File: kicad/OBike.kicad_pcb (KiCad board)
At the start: 4 copper layers, 60 x 99.2 mm, 65 parts, among them J1 62684-402100ALF, J2 Micro_SD_Card_Det1, J3 Conn_01x02, J5 U.FL-R-SMT-1_10_, SW1 5_position_tactile, U1 DPS368XTSA1, U10 MAX40200AUK, U2 DS3231M, U3 MCP23017_SO, U4 74HC14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

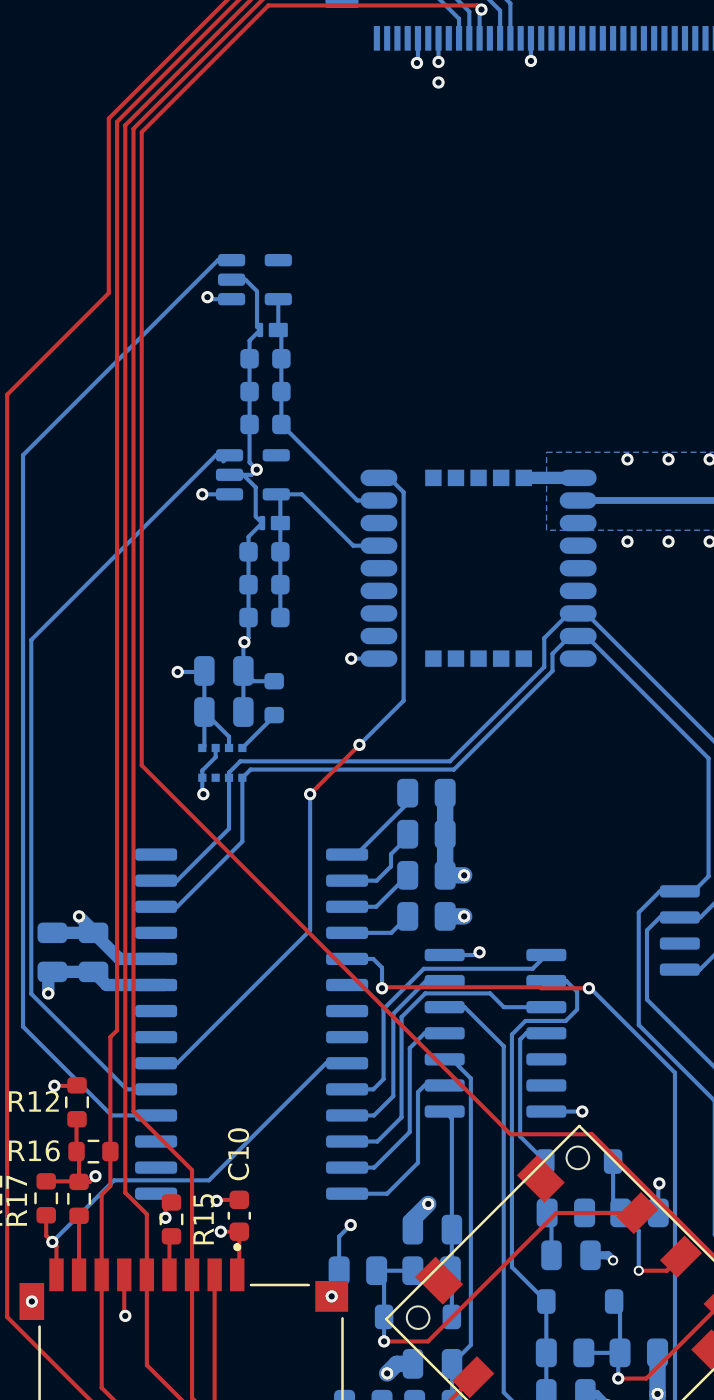
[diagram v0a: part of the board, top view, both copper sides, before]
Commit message: migrate to platform IO
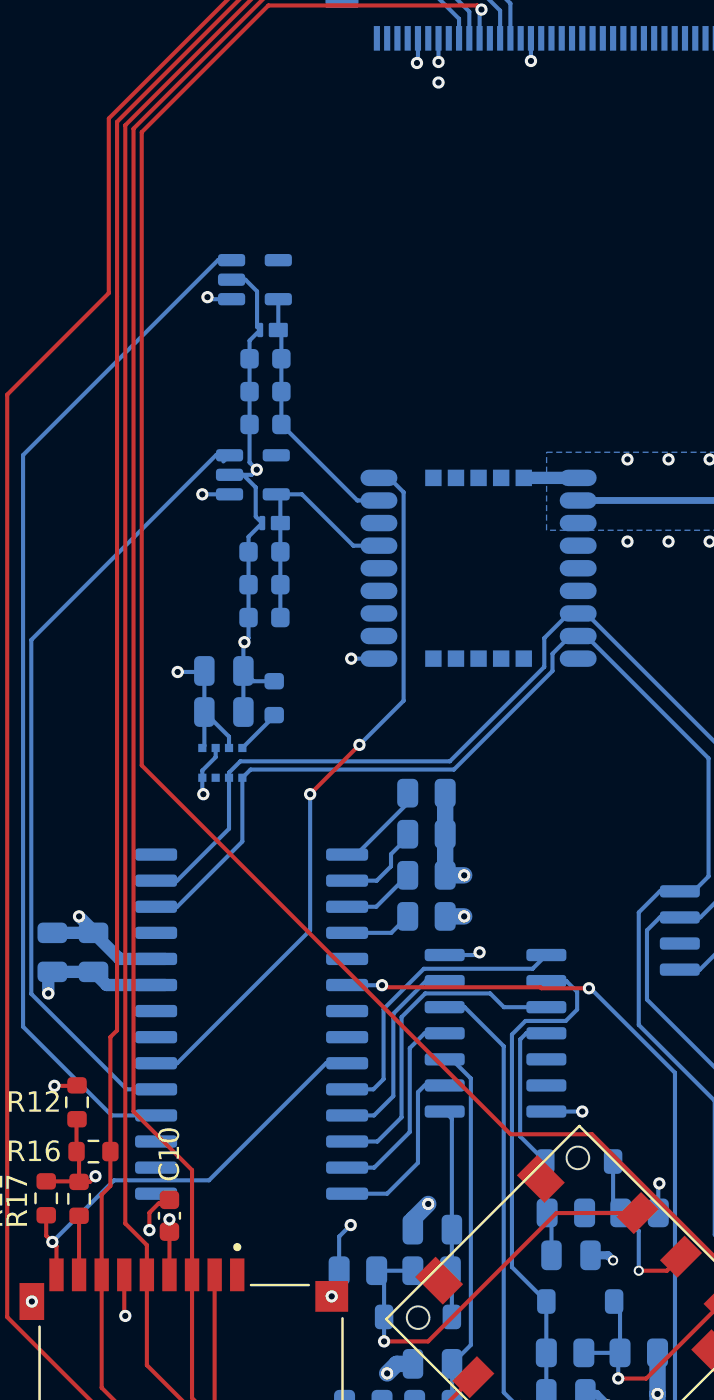
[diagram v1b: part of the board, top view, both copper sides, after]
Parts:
- removed R15: 100K, Resistor_SMD:R_0603_1608Metric
- moved C10 3.40 mm to (128.2, 118.3)
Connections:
- C10 pad 1: Net-(J2-DAT2) -> Net-(J2-VDD)
- J2 pad 1: Net-(J2-DAT2) -> unconnected-(J2-DAT2-Pad1)
- J2 pad CD: CD -> (no net)
- J2 pad G1: GND -> (no net)
- J2 pad G2: GND -> (no net)
- J2 pad G3: GND -> (no net)
- J2 pad G4: GND -> (no net)
- R11 pad 1: Net-(J2-DAT2) -> Net-(J2-VDD)
- R12 pad 2: Net-(J2-DAT2) -> Net-(J2-VDD)
- R16 pad 1: Net-(J2-DAT2) -> Net-(J2-VDD)
- R17 pad 1: Net-(J2-DAT2) -> Net-(J2-VDD)
- U3 pad 19: INT -> unconnected-(U3-INTB-Pad19)
- U3 pad 20: unconnected-(U3-INTA-Pad20) -> INT
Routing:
- net Net-(J2-DAT2): track 16.9 -> 0.00 mm, vias 3 -> 0
- net Net-(J2-VDD): track 2.03 -> 15.7 mm, vias 0 -> 2
- net INT: track 40.1 -> 39.0 mm
- net GND: track 99.5 -> 100.4 mm

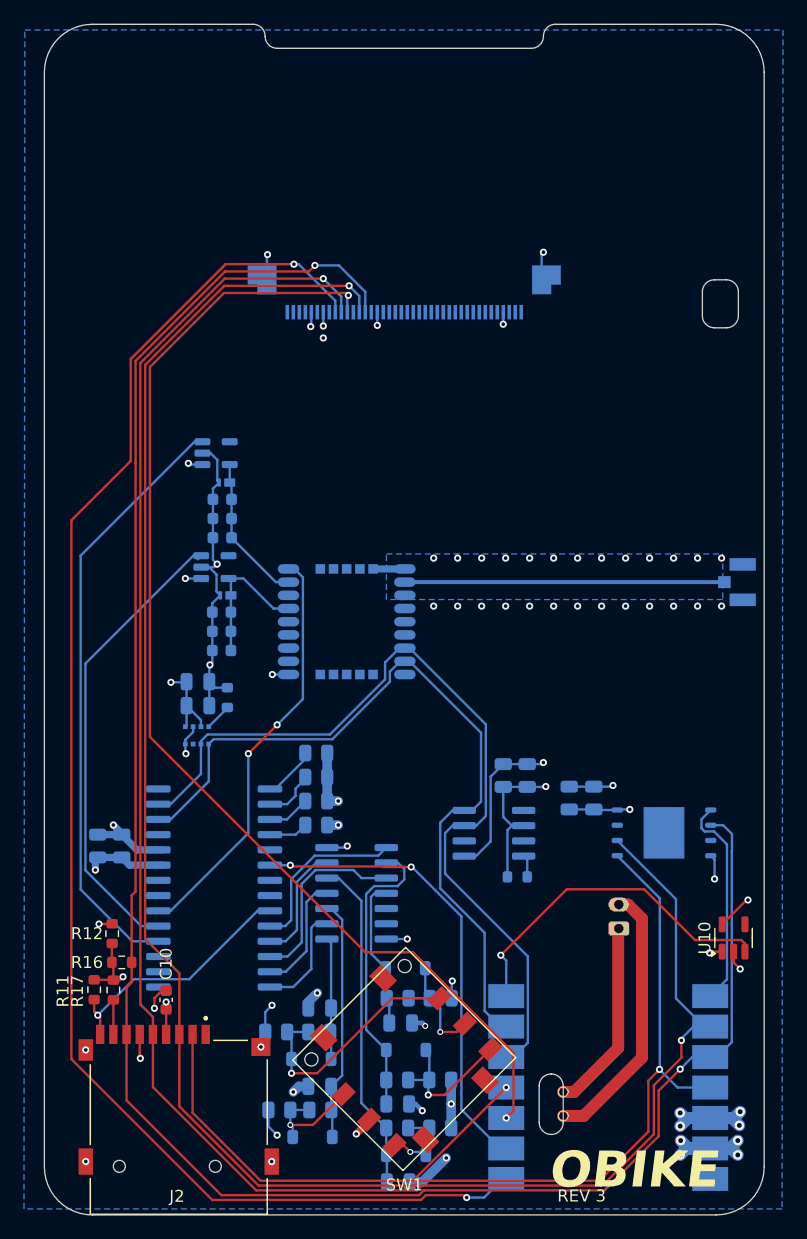
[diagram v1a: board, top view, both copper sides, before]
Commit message: LCD interface
fixed mistakes in FPC connector nets
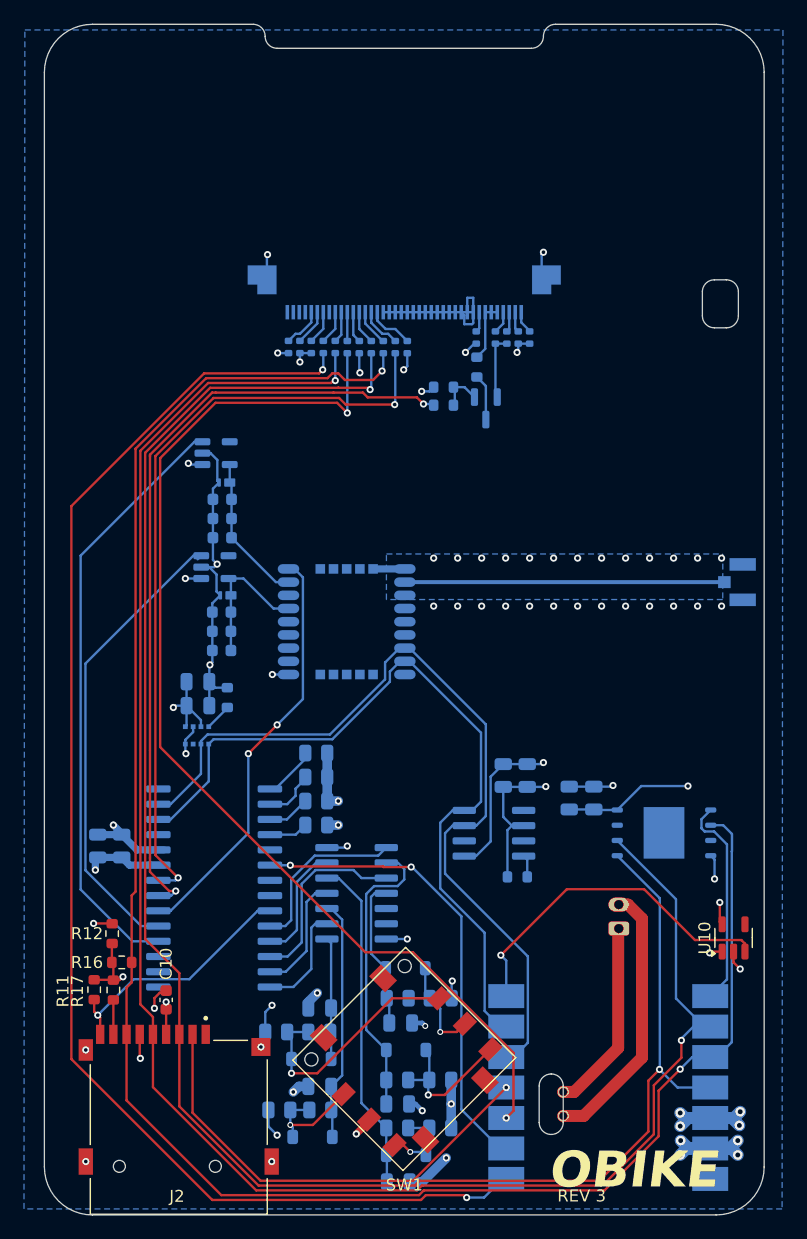
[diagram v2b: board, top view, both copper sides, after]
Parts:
- added Q1: SS8050, Package_TO_SOT_SMD:SOT-23, B.Cu at (154.8, 69.0)
- added R15: 0R, Resistor_SMD:R_0402_1005Metric, B.Cu at (139.3, 63.9)
- added R18: 0R, Resistor_SMD:R_0402_1005Metric, B.Cu at (157.6, 63.1)
- added R19: 0R, Resistor_SMD:R_0402_1005Metric, B.Cu at (158.5, 63.1)
- added R20: 0R, Resistor_SMD:R_0402_1005Metric, B.Cu at (156.6, 63.1)
- added R21: 0R, Resistor_SMD:R_0402_1005Metric, B.Cu at (140.3, 63.9)
- added R26: 0R, Resistor_SMD:R_0402_1005Metric, B.Cu at (141.3, 63.9)
- added R27: 0R, Resistor_SMD:R_0402_1005Metric, B.Cu at (142.3, 63.9)
- added R28: 0R, Resistor_SMD:R_0402_1005Metric, B.Cu at (143.3, 63.9)
- added R29: 0R, Resistor_SMD:R_0402_1005Metric, B.Cu at (144.3, 63.9)
- added R30: 0R, Resistor_SMD:R_0402_1005Metric, B.Cu at (145.3, 63.9)
- added R31: 0R, Resistor_SMD:R_0402_1005Metric, B.Cu at (146.3, 63.9)
- added R32: 0R, Resistor_SMD:R_0402_1005Metric, B.Cu at (147.3, 63.9)
- added R33: 0R, Resistor_SMD:R_0402_1005Metric, B.Cu at (148.3, 63.9)
- added R34: 0R, Resistor_SMD:R_0402_1005Metric, B.Cu at (138.4, 63.9)
- added R35: 0R, Resistor_SMD:R_0402_1005Metric, B.Cu at (155.7, 63.1)
- added R36: 47R, Resistor_SMD:R_0603_1608Metric, B.Cu at (154.1, 65.6)
- added R37: 10K, Resistor_SMD:R_0603_1608Metric, B.Cu at (151.3, 67.2)
- added R38: 1K, Resistor_SMD:R_0603_1608Metric, B.Cu at (151.3, 68.8)
- added R39: 0R, Resistor_SMD:R_0402_1005Metric, B.Cu at (154.1, 63.1)
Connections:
- J1 pad 05: GND -> Net-(J1-Pad05)
- J1 pad 06: unconnected-(J1-Pad06) -> Net-(J1-Pad06)
- J1 pad 07: AUX_3V3 -> Net-(J1-Pad07)
- J1 pad 09: SCR_CS -> Net-(J1-Pad09)
- J1 pad 10: SCK -> Net-(J1-Pad10)
- J1 pad 11: SCR_DC -> Net-(J1-Pad11)
- J1 pad 12: unconnected-(J1-Pad12) -> Net-(J1-Pad12)
- J1 pad 13: MOSI -> Net-(J1-Pad13)
- J1 pad 14: MISO -> Net-(J1-Pad14)
- J1 pad 15: unconnected-(J1-Pad15) -> Net-(J1-Pad15)
- J1 pad 16: GND -> Net-(J1-Pad16)
- J1 pad 17: unconnected-(J1-Pad17) -> GND
- J1 pad 18: unconnected-(J1-Pad18) -> GND
- J1 pad 19: unconnected-(J1-Pad19) -> GND
- J1 pad 20: unconnected-(J1-Pad20) -> GND
- J1 pad 21: unconnected-(J1-Pad21) -> GND
- J1 pad 22: unconnected-(J1-Pad22) -> GND
- J1 pad 23: unconnected-(J1-Pad23) -> GND
- J1 pad 24: unconnected-(J1-Pad24) -> GND
- J1 pad 25: unconnected-(J1-Pad25) -> GND
- J1 pad 26: unconnected-(J1-Pad26) -> GND
- J1 pad 27: unconnected-(J1-Pad27) -> GND
- J1 pad 28: unconnected-(J1-Pad28) -> GND
- J1 pad 29: unconnected-(J1-Pad29) -> GND
- J1 pad 30: unconnected-(J1-Pad30) -> GND
- J1 pad 31: unconnected-(J1-Pad31) -> GND
- J1 pad 32: unconnected-(J1-Pad32) -> GND
- J1 pad 33: unconnected-(J1-Pad33) -> Net-(J1-Pad33)
- J1 pad 34: unconnected-(J1-Pad34) -> Net-(J1-Pad34)
- J1 pad 35: unconnected-(J1-Pad35) -> Net-(J1-Pad34)
- J1 pad 36: unconnected-(J1-Pad36) -> Net-(J1-Pad34)
- J1 pad 37: GND -> Net-(J1-Pad37)
- J1 pad 38: unconnected-(J1-Pad38) -> Net-(J1-Pad38)
- J1 pad 39: unconnected-(J1-Pad39) -> Net-(J1-Pad39)
- J1 pad 40: unconnected-(J1-Pad40) -> Net-(J1-Pad40)
- J2 pad CD: (no net) -> CD
- J2 pad G1: (no net) -> GND
- J2 pad G2: (no net) -> GND
- J2 pad G3: (no net) -> GND
- J2 pad G4: (no net) -> GND
- U3 pad 7: SCR_BL -> SCR_BK
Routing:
- net SCR_BK: track 0.00 -> 65.5 mm, vias 0 -> 2
- net SCR_RST: track 0.00 -> 64.2 mm, vias 0 -> 2
- net AUX_3V3: track 225.5 -> 246.9 mm, vias 5 -> 7
- net GND: track 100.4 -> 121.0 mm, vias 58 -> 59
- net SCR_CS: track 124.9 -> 115.2 mm
- net SCK: track 160.4 -> 152.5 mm
- net MISO: track 167.7 -> 160.5 mm
- net SCR_DC: track 98.3 -> 92.6 mm
- net MOSI: track 158.6 -> 153.2 mm
- net Net-(J1-Pad34): track 0.00 -> 5.04 mm
- net Net-(J1-Pad16): track 0.00 -> 3.90 mm
- net Net-(Q1-C): track 0.00 -> 3.86 mm
- net Net-(Q1-B): track 0.00 -> 3.54 mm
- net Net-(J1-Pad15): track 0.00 -> 3.51 mm
- net Net-(J1-Pad05): track 0.00 -> 3.39 mm
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
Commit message: screen fpc
- changed fpc to bottom mount pins
- changed fpc footprint and symbol
- updated fpc routing
- added JST connectors for SPI & I2C expansion
- stopped tracking kicad/*.zip
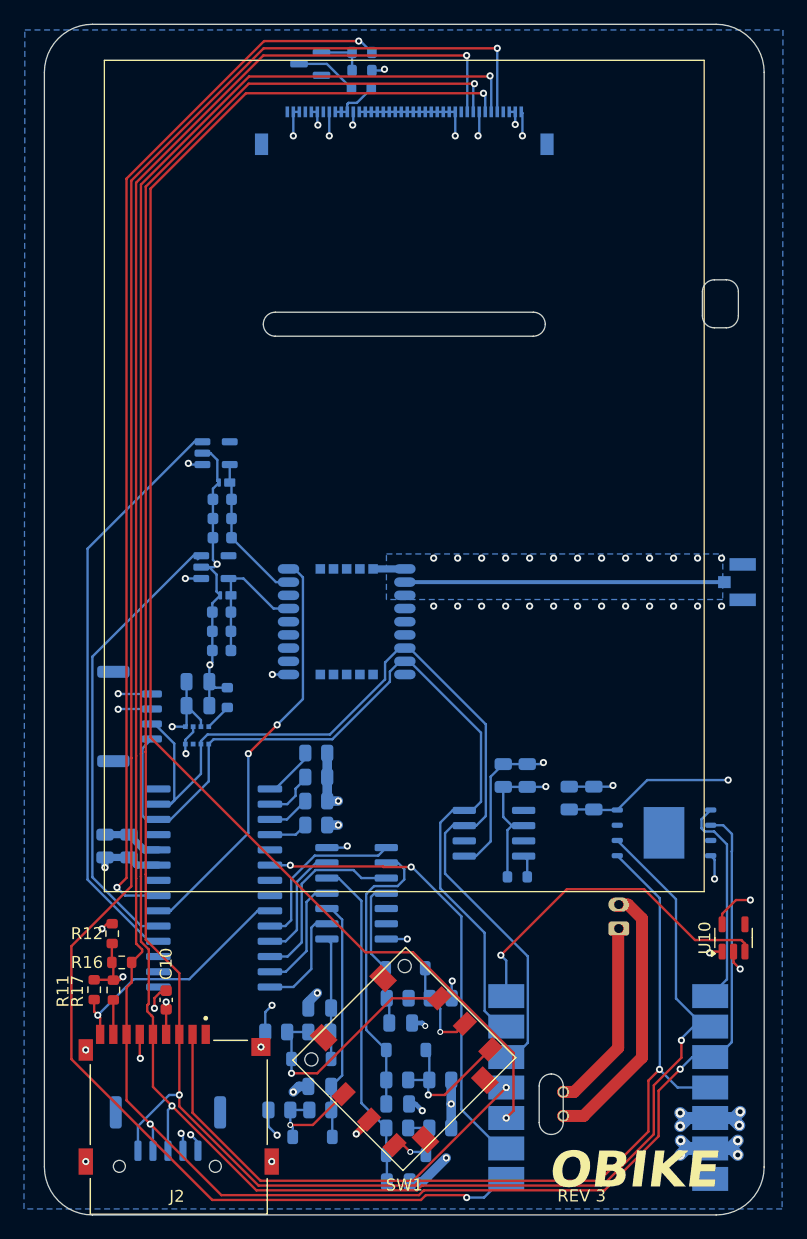
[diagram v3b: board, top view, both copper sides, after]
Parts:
- removed R15, R18, R19, R20, R21, R26, R27, R28, R29, R30, R31, R32, R33, R34, R35, R39: 0R, Resistor_SMD:R_0402_1005Metric
- added J4: Conn_01x04, Connector_JST:JST_GH_SM04B-GHS-TB_1x04-1MP_P1.25mm_Horizontal, B.Cu at (125.2, 94.7)
- added J7: Conn_01x05, Connector_JST:JST_GH_SM05B-GHS-TB_1x05-1MP_P1.25mm_Horizontal, B.Cu at (128.3, 129.1)
- J1: value 62684-402100ALF -> F34G-1A7Q1-E8C40; footprint amphenol:AMPHENOL_62684-402100ALF -> amphenol:AMPHENOL_F34G-1A7Q1-E8C40
- moved Q1 32.2 mm to (140.2, 40.3), turned to 180 degrees
- moved R38 30.2 mm to (144.5, 39.4), turned to 180 degrees
- moved R37 27.3 mm to (144.5, 40.9), turned to 180 degrees
- moved R36 25.1 mm to (144.5, 42.4), turned to 0 degrees
- moved J1 10.4 mm to (148.1, 47.0), turned to 180 degrees
- moved C11 0.60 mm to (125.1, 105.5)
- moved C12 0.60 mm to (123.1, 105.5)
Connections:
- J1 pad 10: Net-(J1-Pad10) -> MISO
- J1 pad 11: Net-(J1-Pad11) -> SCR_RST
- J1 pad 12: Net-(J1-Pad12) -> GND
- J1 pad 13: Net-(J1-Pad13) -> GND
- J1 pad 14: Net-(J1-Pad14) -> GND
- J1 pad 15: Net-(J1-Pad15) -> GND
- J1 pad 16: Net-(J1-Pad16) -> GND
- J1 pad 29: GND -> AUX_3V3
- J1 pad 30: GND -> Net-(J1-Pad30)
- J1 pad 31: GND -> Net-(J1-Pad30)
- J1 pad 32: GND -> Net-(J1-Pad30)
- J1 pad 33: Net-(J1-Pad33) -> GND
- J1 pad 34: Net-(J1-Pad34) -> GND
- J1 pad 35: Net-(J1-Pad34) -> AUX_3V3
- J1 pad 36: Net-(J1-Pad34) -> AUX_3V3
- J1 pad 37: Net-(J1-Pad37) -> unconnected-(J1-Pad37)
- J1 pad 38: Net-(J1-Pad38) -> GND
- J1 pad 39: Net-(J1-Pad39) -> GND
- J1 pad 40: Net-(J1-Pad40) -> unconnected-(J1-Pad40)
- J2 pad CD: CD -> (no net)
- J2 pad G1: GND -> (no net)
- J2 pad G2: GND -> (no net)
- J2 pad G3: GND -> (no net)
- J2 pad G4: GND -> (no net)
- R36 pad 2: Net-(J1-Pad34) -> Net-(J1-Pad30)
- U3 pad 8: SCR_RST -> unconnected-(U3-GPB7-Pad8)
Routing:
- net SCR_RST: track 64.2 -> 0.00 mm, vias 2 -> 0
- net SCR_CS: track 115.2 -> 157.7 mm
- net SCK: track 152.5 -> 193.5 mm, vias 2 -> 3
- net MOSI: track 153.2 -> 191.1 mm, vias 2 -> 3
- net MISO: track 160.5 -> 196.9 mm, vias 2 -> 3
- net SCR_DC: track 92.6 -> 125.2 mm
- net SCR_BK: track 65.5 -> 88.7 mm
- net AUX_3V3: track 246.9 -> 261.5 mm
- net SCL: track 66.6 -> 74.7 mm
- net SDA: track 72.0 -> 79.7 mm
- net GND: track 121.0 -> 115.0 mm, vias 59 -> 60
- net Net-(J1-Pad34): track 5.04 -> 0.00 mm
- net Net-(J1-Pad30): track 0.00 -> 4.19 mm
- net Net-(J1-Pad16): track 3.90 -> 0.00 mm
- net Net-(J1-Pad15): track 3.51 -> 0.00 mm
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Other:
- outline, holes or cut-outs redrawn

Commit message: pcb update
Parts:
- removed the ? at (161.3, 126.0)
- removed the ? at (161.3, 128.0)
- added ?: , , F.Cu at (163.9, 128.0)
- added LS1: PK-11N40PQ, Mallory:PK-11N40PQ_MAL, B.Cu at (123.1, 46.0)
- added REF**: TestPoint_Pad_1.0x1.0mm, TestPoint:TestPoint_Pad_1.0x1.0mm, F.Cu at (163.9, 126.0)
- J4: footprint Connector_JST:JST_GH_SM04B-GHS-TB_1x04-1MP_P1.25mm_Horizontal -> Connector_PinHeader_2.54mm:PinHeader_1x04_P2.54mm_Vertical; moved to F.Cu
- J7: footprint Connector_JST:JST_GH_SM05B-GHS-TB_1x05-1MP_P1.25mm_Horizontal -> Connector_PinHeader_2.54mm:PinHeader_1x05_P2.54mm_Vertical; moved to F.Cu
- moved J7 95.4 mm to (174.0, 45.2), turned to -90 degrees
- moved R12 5.53 mm to (120.7, 117.5), turned to 90 degrees
- moved R16 2.44 mm to (125.3, 117.5), turned to 90 degrees
- moved J4 1.33 mm to (123.8, 94.4), turned to 0 degrees
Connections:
- J1 pad 1: GND -> unconnected-(J1-Pad1)
- J1 pad 10: MISO -> SCK
- J1 pad 11: SCR_RST -> SCR_DC
- J1 pad 13: GND -> MOSI
- J1 pad 14: GND -> MISO
- J1 pad 15: GND -> SCR_RST
- J1 pad 2: AUX_3V3 -> unconnected-(J1-Pad2)
- J1 pad 29: AUX_3V3 -> GND
- J1 pad 3: AUX_3V3 -> unconnected-(J1-Pad3)
- J1 pad 30: Net-(J1-Pad30) -> GND
- J1 pad 31: Net-(J1-Pad30) -> GND
- J1 pad 32: Net-(J1-Pad30) -> GND
- J1 pad 33: GND -> AUX_3V3
- J1 pad 34: GND -> Net-(J1-Pad34)
- J1 pad 35: AUX_3V3 -> Net-(J1-Pad34)
- J1 pad 36: AUX_3V3 -> Net-(J1-Pad34)
- J1 pad 37: unconnected-(J1-Pad37) -> GND
- J1 pad 39: GND -> AUX_3V3
- J1 pad 40: unconnected-(J1-Pad40) -> AUX_3V3
- J1 pad 5: SCR_CS -> GND
- J1 pad 6: SCK -> AUX_3V3
- J1 pad 7: SCR_DC -> AUX_3V3
- J1 pad 8: GND -> unconnected-(J1-Pad8)
- J1 pad 9: MOSI -> SCR_CS
- J4 pad 1: SCL -> SDA
- J4 pad 2: SDA -> SCL
- J7 pad 1: MOSI -> MISO
- J7 pad 2: MISO -> MOSI
- R36 pad 2: Net-(J1-Pad30) -> Net-(J1-Pad34)
- U3 pad 3: unconnected-(U3-GPB2-Pad3) -> BUZZ
- U5 pad 2: INT -> SD_CS
- U5 pad 4: SD_CS -> INT
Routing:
- net BUZZ: track 0.00 -> 73.0 mm
- net MISO: track 196.9 -> 219.6 mm, vias 3 -> 2
- net SCR_DC: track 125.2 -> 139.2 mm
- net MOSI: track 191.1 -> 203.6 mm, vias 3 -> 2
- net SCK: track 193.5 -> 205.7 mm, vias 3 -> 2
- net Net-(J1-Pad34): track 0.00 -> 6.22 mm
- net 3V3: track 49.9 -> 45.5 mm, vias 17 -> 15
- net AUX_3V3: track 261.5 -> 257.1 mm
- net Net-(J1-Pad30): track 4.19 -> 0.00 mm
- net SCR_CS: track 157.7 -> 154.0 mm
- net INT: track 39.0 -> 36.3 mm, vias 2 -> 0
- net SDA: track 79.7 -> 82.2 mm
- net /BAT-: track 22.6 -> 20.8 mm
- net Net-(J2-VDD): track 12.7 -> 14.2 mm
- net SD_CS: track 38.2 -> 36.9 mm
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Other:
- outline, holes or cut-outs redrawn

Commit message: buzzer
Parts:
- added J6: Conn_01x02, Connector_PinHeader_2.00mm:PinHeader_1x02_P2.00mm_Vertical, F.Cu at (163.3, 128.0)
- added Q2: SS8050, Package_TO_SOT_SMD:SOT-23, B.Cu at (127.8, 70.3)
- added R15: 1K, Resistor_SMD:R_0603_1608Metric, B.Cu at (123.7, 70.2)
- added R18: 10K, Resistor_SMD:R_0603_1608Metric, B.Cu at (125.2, 70.2)
- LS1: value PK-11N40PQ -> ASI09N40MTRQ; footprint Mallory:PK-11N40PQ_MAL -> Mallory:ASI09N40M
- moved J4 52.5 mm to (176.2, 98.7)
- moved R38 21.3 mm to (130.2, 55.1), turned to 0 degrees
- moved R37 19.1 mm to (130.2, 53.5), turned to 0 degrees
- moved LS1 16.9 mm to (128.3, 62.1), turned to 90 degrees
- moved R36 15.4 mm to (130.2, 48.3)
- moved Q1 14.6 mm to (130.2, 50.9), turned to 0 degrees
- moved C14 10.5 mm to (172.1, 99.2), turned to 180 degrees
- moved C13 9.29 mm to (172.1, 97.2), turned to 180 degrees
- moved C2 8.08 mm to (152.1, 104.8), turned to -90 degrees
- moved R13 7.83 mm to (153.6, 101.3)
- moved J7 6.30 mm to (175.2, 51.4), turned to 180 degrees
- moved C1 5.63 mm to (154.1, 104.8), turned to -90 degrees
- moved U2 3.57 mm to (158.9, 103.2), turned to 0 degrees
- moved U10 3.18 mm to (175.8, 116.3), turned to -90 degrees
- moved ? 1.98 mm to (165.9, 128.0)
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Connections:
- LS1 pad 1: BUZZ -> AUX_3V3
- LS1 pad 2: GND -> Net-(Q2-C)
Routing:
- net SCR_BK: track 88.7 -> 63.8 mm
- net BUZZ: track 73.0 -> 48.3 mm
- net SCK: track 205.7 -> 224.3 mm
- net GND: track 115.8 -> 97.4 mm, vias 54 -> 59
- net MOSI: track 203.6 -> 221.1 mm
- net AUX_3V3: track 257.1 -> 243.2 mm
- net SCL: track 75.0 -> 85.5 mm, vias 0 -> 1
- net FL_CS: track 18.1 -> 9.70 mm
- net SCR_DC: track 139.2 -> 147.3 mm
- net GPS_RST: track 34.9 -> 42.7 mm, vias 2 -> 0
- net SDA: track 82.2 -> 89.9 mm, vias 0 -> 1
- net Net-(J1-Pad34): track 6.22 -> 13.4 mm
- net Net-(Q2-C): track 0.00 -> 4.48 mm
- net Net-(Q2-B): track 0.00 -> 3.15 mm
- net GPS_VCC: track 12.4 -> 15.3 mm
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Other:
- outline, holes or cut-outs redrawn
